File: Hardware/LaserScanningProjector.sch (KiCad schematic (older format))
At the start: 47 parts, among them J1 5V_IN, J2 SWD, J3 UART, J4 USB_B, J5 LCD, J6 Micro_SD_Card_Det, J7 AUX, SW1 RESET, SW2 BOOT, SW3 5-Way-Navigation-Switch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

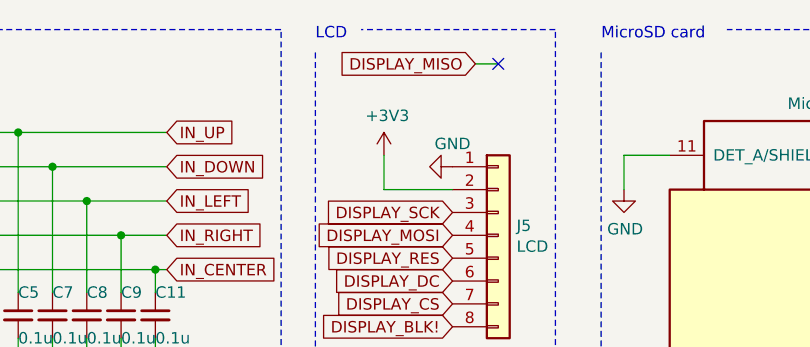
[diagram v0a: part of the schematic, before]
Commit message: Minor changes to hardware
- Changed laser power supply from 3v3 to 5v
   - 5v for more flexibility in laser diode selection
- Bumped revision number to v1.0
- Added version number to PCB
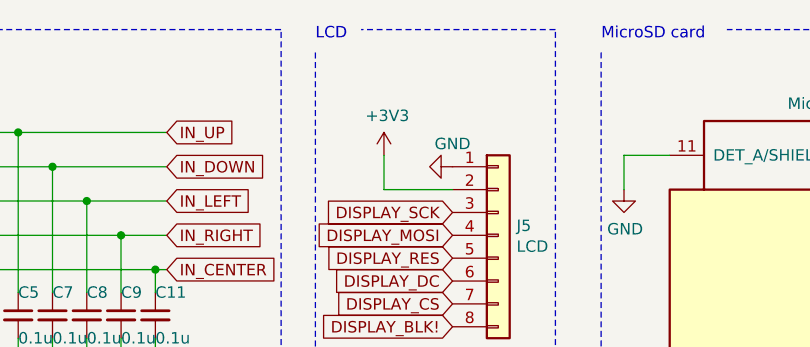
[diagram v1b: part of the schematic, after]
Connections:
- net labels removed: DISPLAY_MISO
- wire segments 159 -> 158
- no-connect marks 5 -> 4
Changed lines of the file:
@@
 Title "Laser Scanning Projector"
 Date ""
-Rev "v0.1"
+Rev "v1.0"
 Comp "ELEC 3300 Group 26"
 Comment1 "Licensed under Creative Commons Attribution-ShareAlike 4.0 International"
@@
 Text GLabel 5500 1400 0    50   Input ~ 0
 DISPLAY_SCK
-Text GLabel 5600 750  0    50   Input ~ 0
-DISPLAY_MISO
 Text GLabel 5500 1500 0    50   Input ~ 0
 DISPLAY_MOSI
@@
 	1    0    0    -1
 $EndComp
-NoConn ~ 5700 750
-Wire Wire Line
-	5700 750  5600 750
 $Comp
 L Connector_Generic:Conn_01x08 J5

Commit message: Swap center and right pins on 5 dir nav switch
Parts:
- renumbered C9 to C11, C11 to C9, R7 to R6, R6 to R7
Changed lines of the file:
@@
 Wire Wire Line
 	3900 1350 3900 1750
-Wire Wire Line
-	4050 1500 4050 1750
-Wire Wire Line
-	4200 1650 4200 1750
 Text GLabel 4250 1050 2    50   Input ~ 0
 IN_UP
@@
 Text GLabel 4250 1350 2    50   Input ~ 0
 IN_LEFT
-Text GLabel 4250 1500 2    50   Input ~ 0
-IN_RIGHT
-Text GLabel 4250 1650 2    50   Input ~ 0
-IN_CENTER
-Wire Wire Line
-	4250 1650 4200 1650
-Wire Wire Line
-	4250 1500 4050 1500
 Wire Wire Line
 	4250 1350 3900 1350
@@
 Text GLabel 4800 3750 0    50   Input ~ 0
 IN_LEFT
-Text GLabel 4800 4950 0    50   Input ~ 0
-IN_RIGHT
-Text GLabel 4800 4850 0    50   Input ~ 0
-IN_CENTER
 Text GLabel 4800 4050 0    50   Input ~ 0
 LDR_DETECT
@@
 	0    1    1    0
 $EndComp
-$Comp
-L Device:R R6
-U 1 1 5DB80642
-P 3350 1500
-F 0 "R6" V 3300 1350 50  0000 C CNN
-F 1 "1k" V 3350 1500 50  0000 C CNN
-F 2 "Resistor_SMD:R_0805_2012Metric_Pad1.15x1.40mm_HandSolder" V 3280 1500 50  0001 C CNN
-F 3 "~" H 3350 1500 50  0001 C CNN
-	1    3350 1500
-	0    1    1    0
-$EndComp
-$Comp
-L Device:R R7
-U 1 1 5DB80912
-P 3350 1650
-F 0 "R7" V 3300 1500 50  0000 C CNN
-F 1 "1k" V 3350 1650 50  0000 C CNN
-F 2 "Resistor_SMD:R_0805_2012Metric_Pad1.15x1.40mm_HandSolder" V 3280 1650 50  0001 C CNN
-F 3 "~" H 3350 1650 50  0001 C CNN
-	1    3350 1650
-	0    1    1    0
-$EndComp
 Wire Wire Line
 	3500 1050 3600 1050
@@
 	3500 1350 3900 1350
 Connection ~ 3900 1350
-Wire Wire Line
-	3500 1500 4050 1500
-Connection ~ 4050 1500
-Wire Wire Line
-	3500 1650 4200 1650
-Connection ~ 4200 1650
 $Comp
 L Device:C_Small C7
@@
 F 3 "~" H 3900 1850 50  0001 C CNN
 	1    3900 1850
-	1    0    0    -1
-$EndComp
-$Comp
-L Device:C_Small C9
-U 1 1 5DBBCF3B
-P 4050 1850
-F 0 "C9" H 4050 1950 50  0000 L CNN
-F 1 "0.1u" H 4050 1750 50  0000 L CNN
-F 2 "Capacitor_SMD:C_0805_2012Metric_Pad1.15x1.40mm_HandSolder" H 4050 1850 50  0001 C CNN
-F 3 "~" H 4050 1850 50  0001 C CNN
-	1    4050 1850
-	1    0    0    -1
-$EndComp
-$Comp
-L Device:C_Small C11
-U 1 1 5DBBD0CA
-P 4200 1850
-F 0 "C11" H 4200 1950 50  0000 L CNN
-F 1 "0.1u" H 4200 1750 50  0000 L CNN
-F 2 "Capacitor_SMD:C_0805_2012Metric_Pad1.15x1.40mm_HandSolder" H 4200 1850 50  0001 C CNN
-F 3 "~" H 4200 1850 50  0001 C CNN
-	1    4200 1850
 	1    0    0    -1
 $EndComp
@@
 EndData
 $EndBitmap
+Text GLabel 4250 1650 2    50   Input ~ 0
+IN_CENTER
+Wire Wire Line
+	3500 1500 4050 1500
+Wire Wire Line
+	4050 1750 4050 1500
+Connection ~ 4050 1500
+Wire Wire Line
+	4050 1500 4250 1500
+Text GLabel 4250 1500 2    50   Input ~ 0
+IN_RIGHT
+Wire Wire Line
+	4200 1650 4200 1750
+Wire Wire Line
+	3500 1650 4200 1650
+Wire Wire Line
+	4200 1650 4250 1650
+Connection ~ 4200 1650
+Text GLabel 4800 4950 0    50   Input ~ 0
+IN_CENTER
+Text GLabel 4800 4850 0    50   Input ~ 0
+IN_RIGHT
+$Comp
+L Device:R R6
+U 1 1 5DB80912
+P 3350 1650
+F 0 "R6" V 3300 1500 50  0000 C CNN
+F 1 "1k" V 3350 1650 50  0000 C CNN
+F 2 "Resistor_SMD:R_0805_2012Metric_Pad1.15x1.40mm_HandSolder" V 3280 1650 50  0001 C CNN
+F 3 "~" H 3350 1650 50  0001 C CNN
+	1    3350 1650
+	0    1    1    0
+$EndComp
+$Comp
+L Device:R R7
+U 1 1 5DB80642
+P 3350 1500
+F 0 "R7" V 3300 1350 50  0000 C CNN
+F 1 "1k" V 3350 1500 50  0000 C CNN
+F 2 "Resistor_SMD:R_0805_2012Metric_Pad1.15x1.40mm_HandSolder" V 3280 1500 50  0001 C CNN
+F 3 "~" H 3350 1500 50  0001 C CNN
+	1    3350 1500
+	0    1    1    0
+$EndComp
+$Comp
+L Device:C_Small C9
+U 1 1 5DBBD0CA
+P 4200 1850
+F 0 "C9" H 4200 1950 50  0000 L CNN
+F 1 "0.1u" H 4200 1750 50  0000 L CNN
+F 2 "Capacitor_SMD:C_0805_2012Metric_Pad1.15x1.40mm_HandSolder" H 4200 1850 50  0001 C CNN
+F 3 "~" H 4200 1850 50  0001 C CNN
+	1    4200 1850
+	1    0    0    -1
+$EndComp
+$Comp
+L Device:C_Small C11
+U 1 1 5DBBCF3B
+P 4050 1850
+F 0 "C11" H 4050 1950 50  0000 L CNN
+F 1 "0.1u" H 4050 1750 50  0000 L CNN
+F 2 "Capacitor_SMD:C_0805_2012Metric_Pad1.15x1.40mm_HandSolder" H 4050 1850 50  0001 C CNN
+F 3 "~" H 4050 1850 50  0001 C CNN
+	1    4050 1850
+	1    0    0    -1
+$EndComp
 $EndSCHEMATC

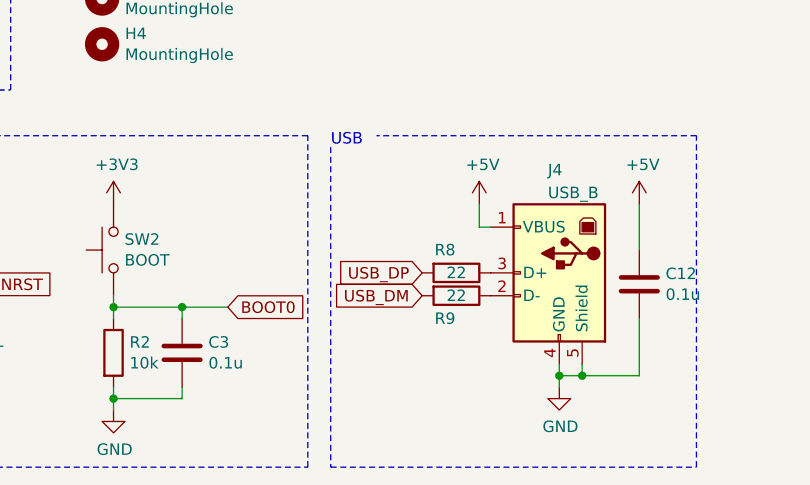
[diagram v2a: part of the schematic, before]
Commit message: Add pull-up resistor to usb dp
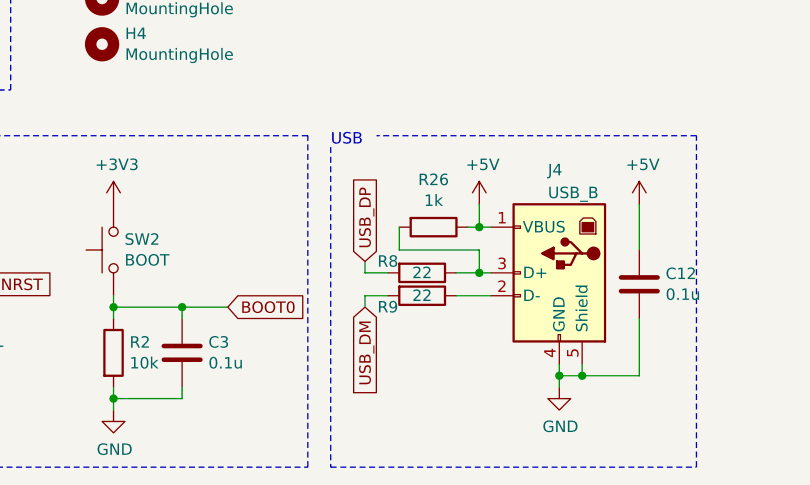
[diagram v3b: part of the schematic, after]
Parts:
- added R26: 1k, Resistor_SMD:R_0805_2012Metric_Pad1.15x1.40mm_HandSolder, symbol Device:R
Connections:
- wire segments 158 -> 169
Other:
- moved on the sheet: R8, R9
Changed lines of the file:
@@
 EESchema Schematic File Version 4
-LIBS:LaserScanningProjector-cache
 EELAYER 30 0
 EELAYER END
@@
 Title "Laser Scanning Projector"
 Date ""
-Rev "v1.0"
+Rev "v1.0.1"
 Comp "ELEC 3300 Group 26"
 Comment1 "Licensed under Creative Commons Attribution-ShareAlike 4.0 International"
@@
 Wire Wire Line
 	3850 7300 3850 7350
-Text GLabel 3250 6850 0    50   Input ~ 0
+Text GLabel 3000 6800 1    50   Input ~ 0
 USB_DP
-Text GLabel 3250 6950 0    50   Input ~ 0
+Text GLabel 3000 7000 3    50   Input ~ 0
 USB_DM
 $Comp
@@
 Connection ~ 3950 7300
 $Comp
-L Device:R R8
-U 1 1 5DD82055
-P 3400 6850
-F 0 "R8" V 3300 6800 50  0000 C CNN
-F 1 "22" V 3400 6850 50  0000 C CNN
-F 2 "Resistor_SMD:R_0805_2012Metric_Pad1.15x1.40mm_HandSolder" V 3330 6850 50  0001 C CNN
-F 3 "~" H 3400 6850 50  0001 C CNN
-	1    3400 6850
-	0    1    1    0
-$EndComp
-$Comp
 L Device:R R9
 U 1 1 5DD89756
-P 3400 6950
-F 0 "R9" V 3500 6900 50  0000 C CNN
-F 1 "22" V 3400 6950 50  0000 C CNN
-F 2 "Resistor_SMD:R_0805_2012Metric_Pad1.15x1.40mm_HandSolder" V 3330 6950 50  0001 C CNN
-F 3 "~" H 3400 6950 50  0001 C CNN
-	1    3400 6950
+P 3250 6950
+F 0 "R9" V 3300 6800 50  0000 C CNN
+F 1 "22" V 3250 6950 50  0000 C CNN
+F 2 "Resistor_SMD:R_0805_2012Metric_Pad1.15x1.40mm_HandSolder" V 3180 6950 50  0001 C CNN
+F 3 "~" H 3250 6950 50  0001 C CNN
+	1    3250 6950
 	0    1    1    0
 $EndComp
@@
 	1    0    0    -1
 $EndComp
+$Comp
+L Device:R R26
+U 1 1 5DD9EBB1
+P 3300 6650
+F 0 "R26" V 3093 6650 50  0000 C CNN
+F 1 "1k" V 3184 6650 50  0000 C CNN
+F 2 "Resistor_SMD:R_0805_2012Metric_Pad1.15x1.40mm_HandSolder" V 3230 6650 50  0001 C CNN
+F 3 "~" H 3300 6650 50  0001 C CNN
+	1    3300 6650
+	0    1    1    0
+$EndComp
+Wire Wire Line
+	3000 6850 3000 6800
+Wire Wire Line
+	3100 6850 3000 6850
+$Comp
+L Device:R R8
+U 1 1 5DD82055
+P 3250 6850
+F 0 "R8" V 3200 6700 50  0000 C CNN
+F 1 "22" V 3250 6850 50  0000 C CNN
+F 2 "Resistor_SMD:R_0805_2012Metric_Pad1.15x1.40mm_HandSolder" V 3180 6850 50  0001 C CNN
+F 3 "~" H 3250 6850 50  0001 C CNN
+	1    3250 6850
+	0    1    1    0
+$EndComp
+Wire Wire Line
+	3100 6950 3000 6950
+Wire Wire Line
+	3000 6950 3000 7000
+Wire Wire Line
+	3400 6950 3550 6950
+Wire Wire Line
+	3400 6850 3500 6850
+Wire Wire Line
+	3150 6650 3150 6750
+Wire Wire Line
+	3150 6750 3500 6750
+Wire Wire Line
+	3500 6750 3500 6850
+Connection ~ 3500 6850
+Wire Wire Line
+	3500 6850 3550 6850
+Wire Wire Line
+	3450 6650 3500 6650
+Connection ~ 3500 6650
 $EndSCHEMATC
